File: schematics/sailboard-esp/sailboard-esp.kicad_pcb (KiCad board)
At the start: 2 copper layers, 91.4 x 51.4 mm, 40 parts, among them IC1 TXB0108PWR, U1 AP2112K-3.3, U2 L293D

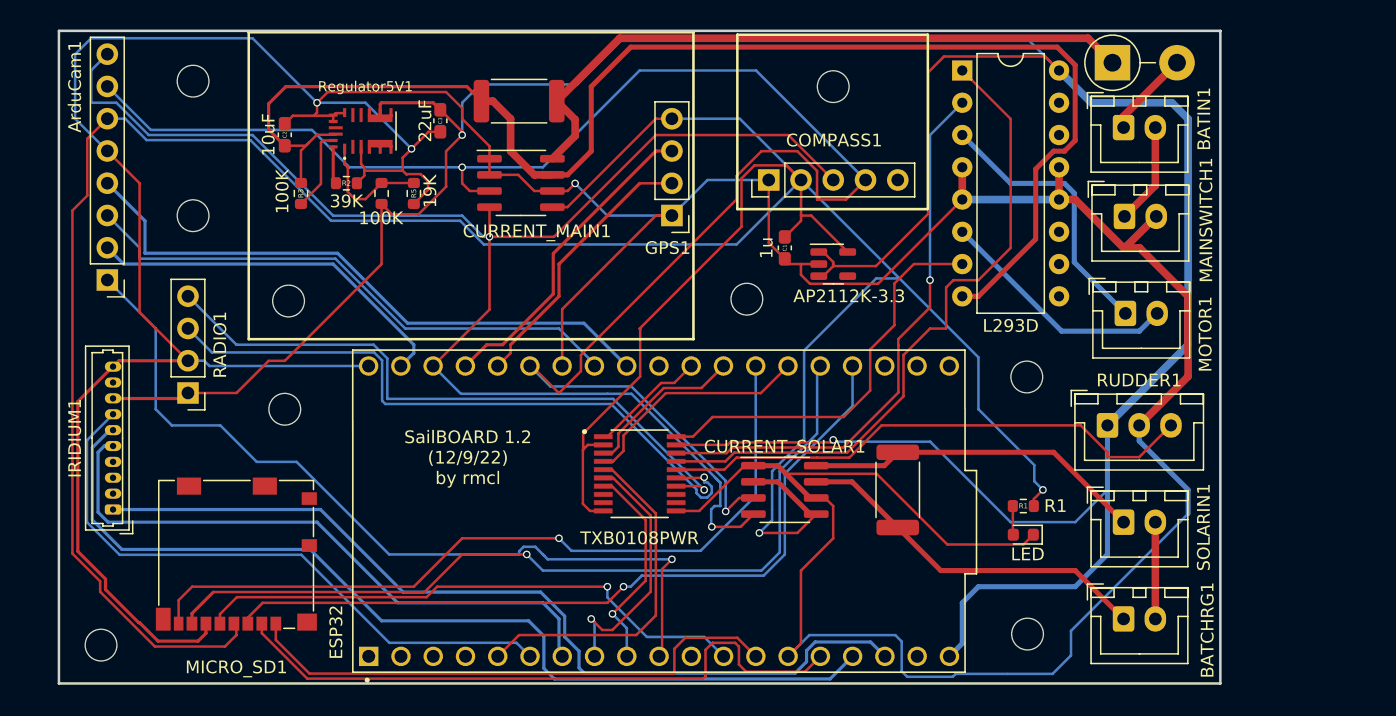
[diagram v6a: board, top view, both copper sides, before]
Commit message: more tweaks. Add mounting holes for rockblock.
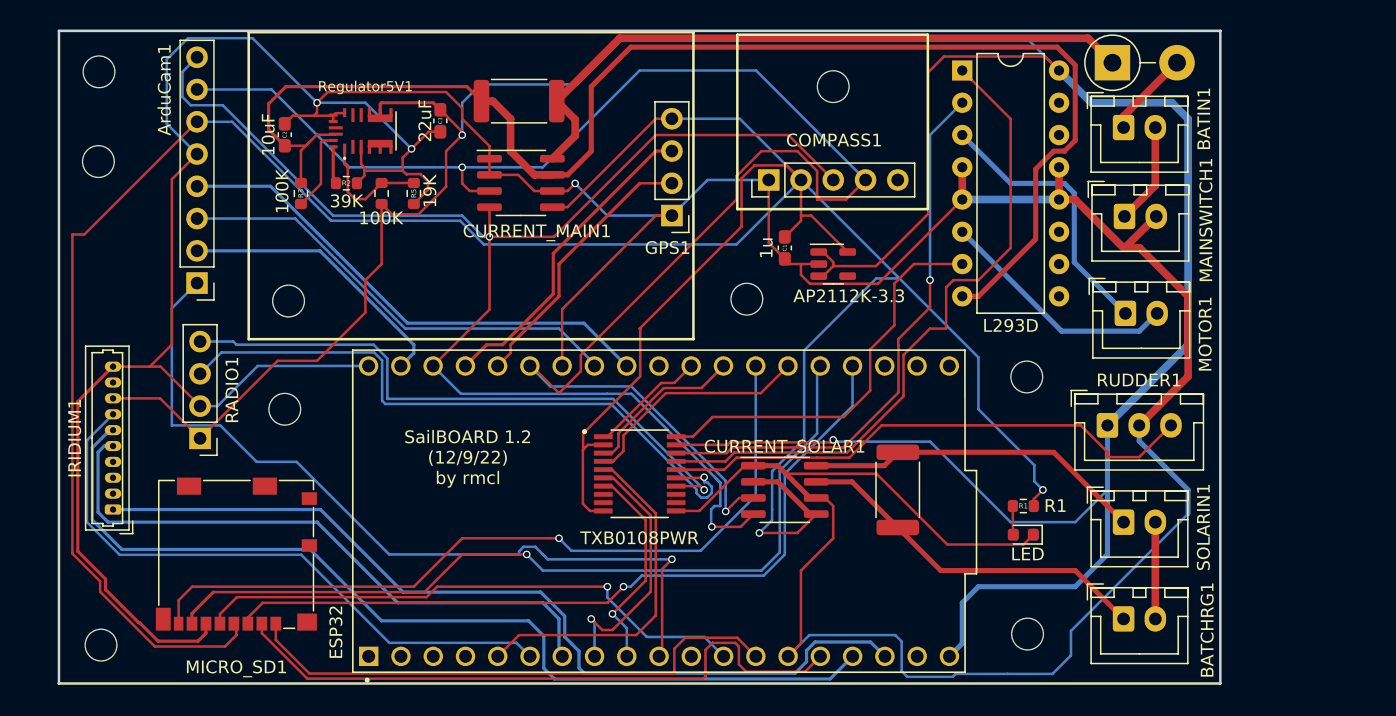
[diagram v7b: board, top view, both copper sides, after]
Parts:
- moved H1 8.59 mm to (155.5, 32.8)
- moved H1 7.44 mm to (155.6, 25.8)
- moved ArduCam1 7.07 mm to (163.3, 42.4)
- moved RADIO1 3.70 mm to (163.5, 54.6)
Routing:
- net /SCK: track 48.3 -> 39.7 mm
- net /SCL: track 120.9 -> 113.2 mm
- net /MISO: track 43.7 -> 36.0 mm
- net /MOSI: track 29.4 -> 22.2 mm
- net /SDA: track 137.5 -> 130.3 mm
- net GND: track 359.0 -> 353.1 mm
- net +5V: track 241.7 -> 245.8 mm
- net +3.3V: track 258.9 -> 255.0 mm
- net /RADIO_CHAN2_5V: track 51.2 -> 48.7 mm
- net /ARDUCAM_CS: track 66.2 -> 64.6 mm
- net /RADIO_CHAN1_5V: track 52.8 -> 51.8 mm

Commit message: tweaks.
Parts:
- C1: value 1u -> 1uF
- R2: value 39K -> 53.6K
- R5: value 19K -> 19.1K
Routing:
- net /ARDUCAM_CS: track 64.6 -> 66.8 mm
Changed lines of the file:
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@@
       (usegerberattributes true)
       (usegerberadvancedattributes true)
-      (creategerberjobfile true)
+      (creategerberjobfile false)
       (svguseinch false)
       (svgprecision 6)
@@
     (fp_line (start 4.95 3.4) (end 4.95 -2.35) (layer "F.Fab") (width 0.1))
     (fp_line (start 0 -1.35) (end 0.625 -2.35) (layer "F.Fab") (width 0.1))
-    (pad "1" thru_hole roundrect (at 0 0) (size 1.7 2) (drill 1) (layers *.Cu *.Mask) (roundrect_rratio 0.147059)
+    (pad "1" thru_hole roundrect (at 0 0) (size 1.7 2) (drill 1) (layers *.Cu *.Mask) (roundrect_rratio 0.1470588235)
       (net 12 "/Power/Battery Input") (pinfunction "Pin_1") (pintype "passive"))
     (pad "2" thru_hole oval (at 2.5 0) (size 1.7 2) (drill 1) (layers *.Cu *.Mask)
@@
     (fp_line (start 4.95 -2.35) (end -2.45 -2.35) (layer "F.Fab") (width 0.1))
     (fp_line (start -0.625 -2.35) (end 0 -1.35) (layer "F.Fab") (width 0.1))
-    (pad "1" thru_hole roundrect (at 0 0) (size 1.7 2) (drill 1) (layers *.Cu *.Mask) (roundrect_rratio 0.147059)
+    (pad "1" thru_hole roundrect (at 0 0) (size 1.7 2) (drill 1) (layers *.Cu *.Mask) (roundrect_rratio 0.1470588235)
       (net 45 "/Power/Solar Pos") (pinfunction "Pin_1") (pintype "passive"))
     (pad "2" thru_hole oval (at 2.5 0) (size 1.7 2) (drill 1) (layers *.Cu *.Mask)
@@
       (effects (font (size 1 1) (thickness 0.15)))
     )
-    (fp_text value "19K" (at -0.169861 -1.29248 -90) (layer "F.SilkS")
+    (fp_text value "19.1K" (at -0.169861 -1.29248 -90) (layer "F.SilkS")
       (effects (font (size 1 1) (thickness 0.15)))
     )
@@
     (fp_line (start -0.625 -2.35) (end 0 -1.35) (layer "F.Fab") (width 0.1))
     (fp_line (start -2.45 3.4) (end 4.95 3.4) (layer "F.Fab") (width 0.1))
-    (pad "1" thru_hole roundrect (at 0 0) (size 1.7 2) (drill 1) (layers *.Cu *.Mask) (roundrect_rratio 0.147059)
+    (pad "1" thru_hole roundrect (at 0 0) (size 1.7 2) (drill 1) (layers *.Cu *.Mask) (roundrect_rratio 0.1470588235)
       (net 13 "Net-(BATIN1-Pad2)") (pinfunction "Pin_1") (pintype "passive"))
     (pad "2" thru_hole oval (at 2.5 0) (size 1.7 2) (drill 1) (layers *.Cu *.Mask)
@@
       (effects (font (size 1 1) (thickness 0.15)))
     )
-    (fp_text value "1u" (at 0 1.43 90) (layer "F.SilkS")
+    (fp_text value "1uF" (at 0 1.43 90) (layer "F.SilkS")
       (effects (font (size 1 1) (thickness 0.15)))
     )
@@
     (fp_line (start -2.45 3.4) (end 7.45 3.4) (layer "F.Fab") (width 0.1))
     (fp_line (start 7.45 -2.35) (end -2.45 -2.35) (layer "F.Fab") (width 0.1))
-    (pad "1" thru_hole roundrect (at 0 0) (size 1.7 1.95) (drill 0.95) (layers *.Cu *.Mask) (roundrect_rratio 0.147059)
+    (pad "1" thru_hole roundrect (at 0 0) (size 1.7 1.95) (drill 0.95) (layers *.Cu *.Mask) (roundrect_rratio 0.1470588235)
       (net 1 "+5V") (pinfunction "Pin_1") (pintype "passive"))
     (pad "2" thru_hole oval (at 2.5 0) (size 1.7 1.95) (drill 0.95) (layers *.Cu *.Mask)
@@
     (fp_line (start -2.45 3.4) (end 4.95 3.4) (layer "F.Fab") (width 0.1))
     (fp_line (start 4.95 -2.35) (end -2.45 -2.35) (layer "F.Fab") (width 0.1))
-    (pad "1" thru_hole roundrect (at 0 0) (size 1.7 2) (drill 1) (layers *.Cu *.Mask) (roundrect_rratio 0.147059)
+    (pad "1" thru_hole roundrect (at 0 0) (size 1.7 2) (drill 1) (layers *.Cu *.Mask) (roundrect_rratio 0.1470588235)
       (net 23 "Net-(MOTOR1-Pad1)") (pinfunction "Pin_1") (pintype "passive"))
     (pad "2" thru_hole oval (at 2.5 0) (size 1.7 2) (drill 1) (layers *.Cu *.Mask)
@@
     (fp_line (start -0.625 -2.35) (end 0 -1.35) (layer "F.Fab") (width 0.1))
     (fp_line (start 4.95 -2.35) (end -2.45 -2.35) (layer "F.Fab") (width 0.1))
-    (pad "1" thru_hole roundrect (at 0 0) (size 1.7 2) (drill 1) (layers *.Cu *.Mask) (roundrect_rratio 0.147059)
+    (pad "1" thru_hole roundrect (at 0 0) (size 1.7 2) (drill 1) (layers *.Cu *.Mask) (roundrect_rratio 0.1470588235)
       (net 44 "/Power/Battery Charge Pos") (pinfunction "Pin_1") (pintype "passive"))
     (pad "2" thru_hole oval (at 2.5 0) (size 1.7 2) (drill 1) (layers *.Cu *.Mask)
@@
       (effects (font (size 1 1) (thickness 0.15)))
     )
-    (fp_text user "${REFERENCE}" (at 0 0 90) (layer "F.Fab")
+    (fp_text user "${REFERENCE}" (at 0 0 90) (layer "F.SilkS")
       (effects (font (size 0.4 0.4) (thickness 0.06)))
     )
@@
       (effects (font (size 1 1) (thickness 0.15)))
     )
-    (fp_text value "39K" (at 0 1.43) (layer "F.SilkS")
+    (fp_text value "53.6K" (at 0 1.43) (layer "F.SilkS")
       (effects (font (size 1 1) (thickness 0.15)))
     )
@@
   (segment (start 172.72 48.53) (end 176.53 44.72) (width 0.2) (layer "F.Cu") (net 1))
   (segment (start 182.88 32.02) (end 184.15 30.75) (width 0.2) (layer "F.Cu") (net 1))
-  (segment (start 156.66 51.485) (end 156.669707 51.494707) (width 0.25) (layer "F.Cu") (net 1))
   (segment (start 163.512481 54.63217) (end 160.365311 51.485) (width 0.2) (layer "F.Cu") (net 1))
   (segment (start 182.429399 28.76832) (end 181.871079 28.21) (width 0.25) (layer "F.Cu") (net 1))
@@
   (via (at 200.66 64.154887) (size 0.6) (drill 0.4) (layers "F.Cu" "B.Cu") (net 62))
   (segment (start 161.29 44.391628) (end 163.274343 42.407285) (width 0.2) (layer "B.Cu") (net 62))
+  (segment (start 190.884887 64.154887) (end 190.5 63.77) (width 0.2) (layer "B.Cu") (net 62))
+  (segment (start 189.9 63.17) (end 188.981471 63.17) (width 0.2) (layer "B.Cu") (net 62))
+  (segment (start 167.97448 56.48448) (end 167.640194 56.818766) (width 0.2) (layer "B.Cu") (net 62))
+  (segment (start 188.63 63.77) (end 178.401041 63.77) (width 0.2) (layer "B.Cu") (net 62))
+  (segment (start 167.640194 56.818766) (end 161.29 56.818766) (width 0.2) (layer "B.Cu") (net 62))
+  (segment (start 161.29 56.818766) (end 161.29 44.391628) (width 0.2) (layer "B.Cu") (net 62))
+  (segment (start 188.63 63.521471) (end 188.63 63.77) (width 0.2) (layer "B.Cu") (net 62))
+  (segment (start 190.617157 63.887157) (end 189.9 63.17) (width 0.2) (layer "B.Cu") (net 62))
+  (segment (start 178.401041 63.77) (end 171.11552 56.48448) (width 0.2) (layer "B.Cu") (net 62))
   (segment (start 171.11552 56.48448) (end 167.97448 56.48448) (width 0.2) (layer "B.Cu") (net 62))
-  (segment (start 190.884887 64.154887) (end 190.5 63.77) (width 0.2) (layer "B.Cu") (net 62))
-  (segment (start 161.29 53.61) (end 161.29 44.391628) (width 0.2) (layer "B.Cu") (net 62))
-  (segment (start 188.63 63.521471) (end 188.981471 63.17) (width 0.2) (layer "B.Cu") (net 62))
-  (segment (start 167.97448 56.48448) (end 165.1 53.61) (width 0.2) (layer "B.Cu") (net 62))
-  (segment (start 189.9 63.17) (end 190.617157 63.887157) (width 0.2) (layer "B.Cu") (net 62))
-  (segment (start 188.981471 63.17) (end 189.9 63.17) (width 0.2) (layer "B.Cu") (net 62))
-  (segment (start 171.11552 56.48448) (end 178.401041 63.77) (width 0.2) (layer "B.Cu") (net 62))
-  (segment (start 165.1 53.61) (end 161.29 53.61) (width 0.2) (layer "B.Cu") (net 62))
+  (segment (start 188.981471 63.17) (end 188.63 63.521471) (width 0.2) (layer "B.Cu") (net 62))
   (segment (start 200.66 64.154887) (end 190.884887 64.154887) (width 0.2) (layer "B.Cu") (net 62))
-  (segment (start 178.401041 63.77) (end 188.63 63.77) (width 0.2) (layer "B.Cu") (net 62))
-  (segment (start 188.63 63.77) (end 188.63 63.521471) (width 0.2) (layer "B.Cu") (net 62))
   (segment (start 195.942841 57.095) (end 195.25 57.095) (width 0.2) (layer "F.Cu") (net 66))
   (segment (start 186.95 71.795) (end 188.625 70.12) (width 0.2) (layer "F.Cu") (net 66))
